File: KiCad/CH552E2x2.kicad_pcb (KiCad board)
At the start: 2 copper layers, 49 x 35.6 mm, 22 parts, among them J1 USB_C_Receptacle_USB2.0, U1 CH552E, U2 PRTR5V0U2X

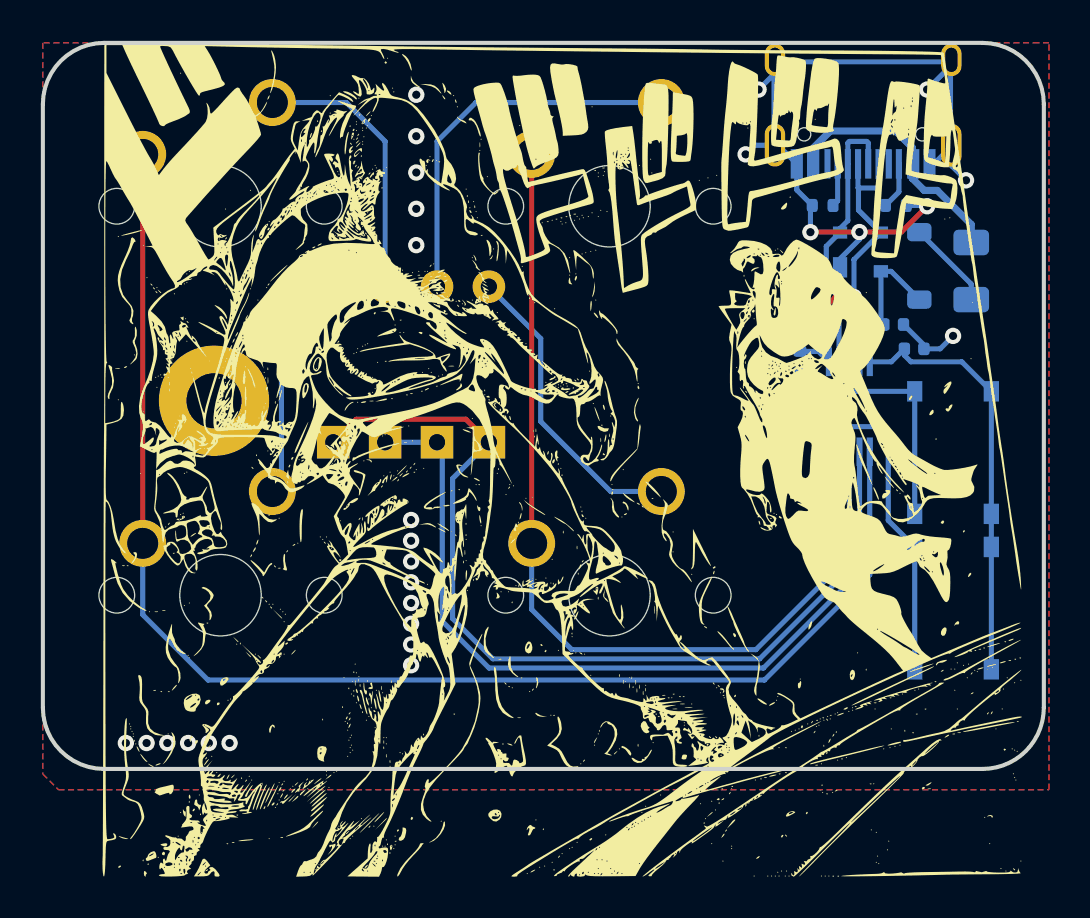
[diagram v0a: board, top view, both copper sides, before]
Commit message: Remove Silkscreen
Removed Silkscreen
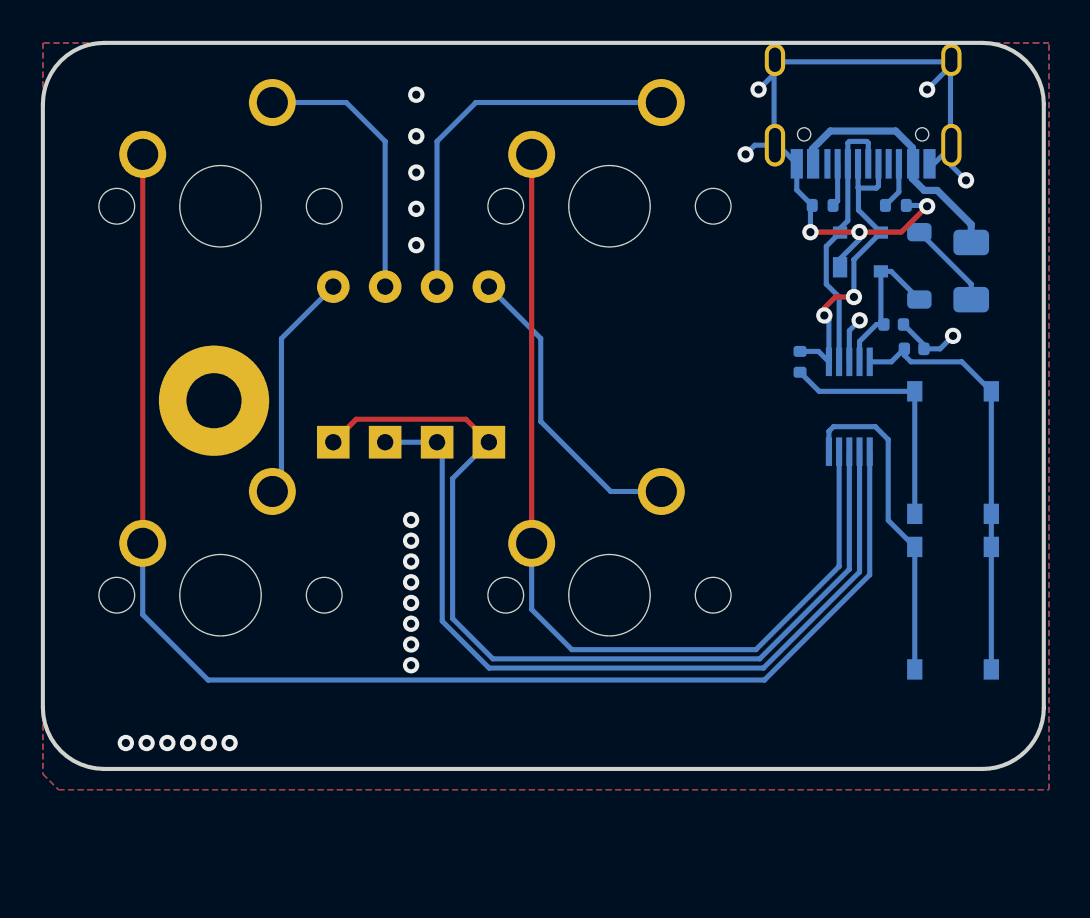
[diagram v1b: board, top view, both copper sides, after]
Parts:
- removed G***: LOGO, LOGO

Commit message: Update
Solder -> Hot Swap
THT -> SMD Diodes
Screw Hole -> Not Inconvenient Anymore
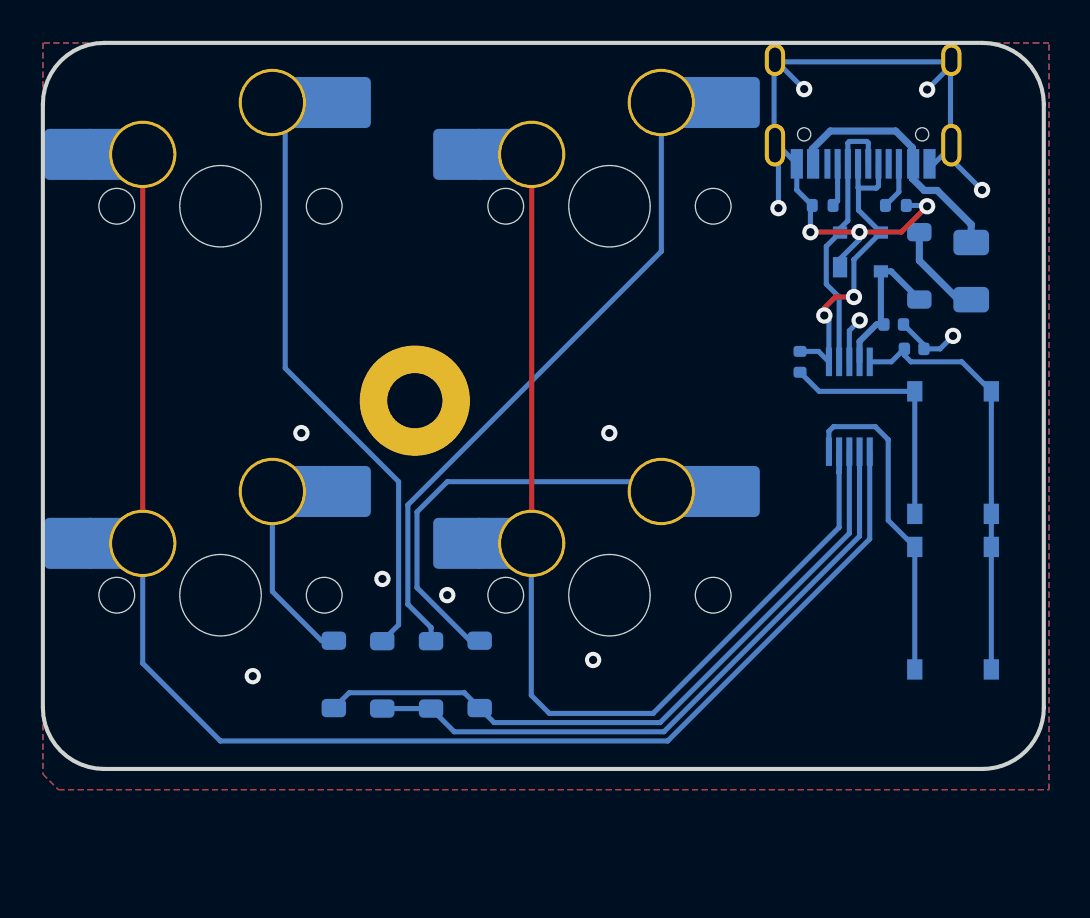
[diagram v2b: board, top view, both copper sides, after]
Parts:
- D3, D4, D5, D6: footprint VyPrints:D_DO-35_SOD27_P7.62mm_Horizontal -> Diode_SMD:D_SOD-123
- MX1, MX2, MX3, MX4: footprint PCM_marbastlib-mx_1:SW_MX_1u -> PCM_marbastlib-mx:SW_MX_HS_CPG151101S11_1u; moved to B.Cu
- moved D4 11.4 mm to (107.1, 64.2)
- moved D3 11.4 mm to (104.8, 64.2)
- moved D6 11.4 mm to (109.5, 64.2)
- moved D5 11.4 mm to (102.4, 64.2)
- moved H1 9.84 mm to (106.4, 50.8)
- turned MX1 to 180 degrees
- turned MX2 to 180 degrees
- turned MX3 to 180 degrees
- turned MX4 to 180 degrees
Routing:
- net Net-(D3-A): track 13.4 -> 29.3 mm
- net Net-(D4-A): track 18.9 -> 32.0 mm
- net ROW1: track 45.7 -> 34.0 mm
- net ROW0: track 40.3 -> 32.0 mm
- net Net-(D6-A): track 15.0 -> 20.6 mm
- net COL1: track 45.5 -> 50.5 mm
- net COL0: track 67.6 -> 70.5 mm
- net GND: track 45.6 -> 48.1 mm, vias 28 -> 15
- net Net-(D5-A): track 10.6 -> 8.91 mm
